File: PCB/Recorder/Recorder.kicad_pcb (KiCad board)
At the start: 2 copper layers, 70 x 70 mm, 54 parts, among them J1 Battery, J2 Reset, J3 TC2030-USB-NL-DS, J4 TF_PUSH, J5 USB-C-Socket-H, Q2 CJ2301, SW1 SW_Push, U1 R, U2 L, U3 TP4054, U4 ME6211C33M5G-N, U5 MAX98357A, U6 ESP32-S3-MINI-1

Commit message: Allow all data on SD card maybe
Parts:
- R14: moved to F.Cu
- moved R14 16.2 mm to (94.0, 108.8), turned to 90 degrees
- moved R10 0.85 mm to (97.5, 108.8)
- moved R13 0.85 mm to (94.9, 108.8)
- moved R3 0.85 mm to (99.2, 108.8)
- moved R11 0.85 mm to (96.6, 108.8)
- moved R12 0.85 mm to (95.8, 108.8)
- moved R9 0.85 mm to (98.3, 108.8)
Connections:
- J4 pad 1: Net-(J4-DAT2) -> SDDAT2
- R14 pad 2: Net-(J4-DAT2) -> SDDAT2
- U6 pad 15: unconnected-(U6-GPIO11-Pad15) -> CHARGING
- U6 pad 16: SDSS -> SDDAT2
- U6 pad 17: SDMOSI -> SDSS
- U6 pad 18: SDSCK -> SDMOSI
- U6 pad 19: SDMISO -> SDSCK
- U6 pad 20: SDDAT1 -> SDMISO
- U6 pad 21: SDCD -> SDDAT1
- U6 pad 22: CHARGING -> SDCD
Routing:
- net SDDAT2: track 0.00 -> 18.1 mm, vias 0 -> 1
- net GND: track 59.6 -> 71.6 mm, vias 17 -> 21
- net CHARGING: track 20.3 -> 27.9 mm, vias 2 -> 4
- net Net-(J2-Pin_2): track 24.8 -> 29.3 mm
- net +3V3: track 135.7 -> 133.4 mm
- net Net-(J4-DAT2): track 1.22 -> 0.00 mm
- net SDCD: track 24.9 -> 25.6 mm
- net D+: track 28.7 -> 28.2 mm

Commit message: Tidy
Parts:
- removed C12: 10uF, RevK:C_0402
- removed C14: 100nF, RevK:C_0402
- removed R4: 634K, RevK:R_0402
- removed TP1: +, RevK:SolderPadSmall
- removed TP2: -, RevK:SolderPadSmall
- removed U5: MAX98357A, RevK:WLP-1.437mmx1.347mm-0.21mm-ball
- moved V2 1.50 mm to (96.5, 110.0)
- moved PCB1 1.00 mm to (96.0, 100.0)
- moved V1 1.00 mm to (96.0, 90.0)
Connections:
- net SDMISO renamed SDDAT0
- net SDMOSI renamed SDCMD
- net SDSCK renamed SDCLK
- net SDSS renamed SDDAT3
- U6 pad 31: SKPWS -> unconnected-(U6-GPIO35-Pad31)
- U6 pad 32: SKPSCK -> unconnected-(U6-GPIO36-Pad32)
- U6 pad 33: SKPSD -> unconnected-(U6-GPIO37-Pad33)
- U6 pad 34: SKPPWR -> unconnected-(U6-GPIO38-Pad34)
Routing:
- net SKPPWR: track 6.62 -> 0.00 mm
- net GND: track 71.6 -> 65.1 mm, vias 21 -> 20
- net SKPWS: track 4.62 -> 0.00 mm, vias 2 -> 0
- net Net-(U5-OUTN): track 4.43 -> 0.00 mm, vias 1 -> 0
- net SKPSD: track 3.77 -> 0.00 mm
- net SKPSCK: track 2.42 -> 0.00 mm
- net +3V3: track 133.4 -> 131.6 mm
- net SCK: track 37.2 -> 35.9 mm
- net SDCD: track 25.6 -> 24.4 mm
- net CHARGING: track 27.9 -> 29.0 mm
- net Net-(U5-OUTP): track 1.02 -> 0.00 mm, vias 1 -> 0
- net D-: track 37.5 -> 36.4 mm
- net Net-(U5-~{SD_MODE}): track 0.60 -> 0.00 mm
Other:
- board text added: "1 8"
- board text added: "12 13 14 15 16 17 18"
- board text added: "41 18"
- board text added: "BTN LED"
- board text added: "Baking not required"
- board text added: "DAT2 DAT3 MOSI SCK DAT0 DAT1 CD"
- board text added: "VBUS CHRG"
- board text added: "Voice Recorder"
- board text removed: "1"
- board text removed: "12 13 14 15 17"
- board text removed: "18"
- board text removed: "35 36"
- board text removed: "37 38"
- board text removed: "41"
- board text removed: "8"
- board text removed: "A"
- board text removed: "Audio"
- board text removed: "B"
- board text removed: "BTN"
- board text removed: "Baking for D1 is not required"
- board text removed: "CHG"
- board text removed: "D P"
- board text removed: "Recorder"
- board text removed: "SPK"
- board text removed: "SS MOSI SCK MISO CD"
- board text removed: "VBUS"
- board text removed: "W C"

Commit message: Clean up
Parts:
- moved C13 5.29 mm to (87.5, 105.5)
- moved C8 3.24 mm to (90.0, 94.5)
- moved J2 2.35 mm to (82.5, 94.0)
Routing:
- net GND: track 65.1 -> 55.3 mm
- net +3V3: track 131.6 -> 122.4 mm
- net Net-(J2-Pin_2): track 29.3 -> 30.9 mm
- net SCK: track 35.9 -> 34.4 mm, vias 2 -> 3
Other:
- board text added: "1"
- board text added: "8"
- board text removed: "1 8"
- board text removed: "BTN LED"
- board text removed: "LED"

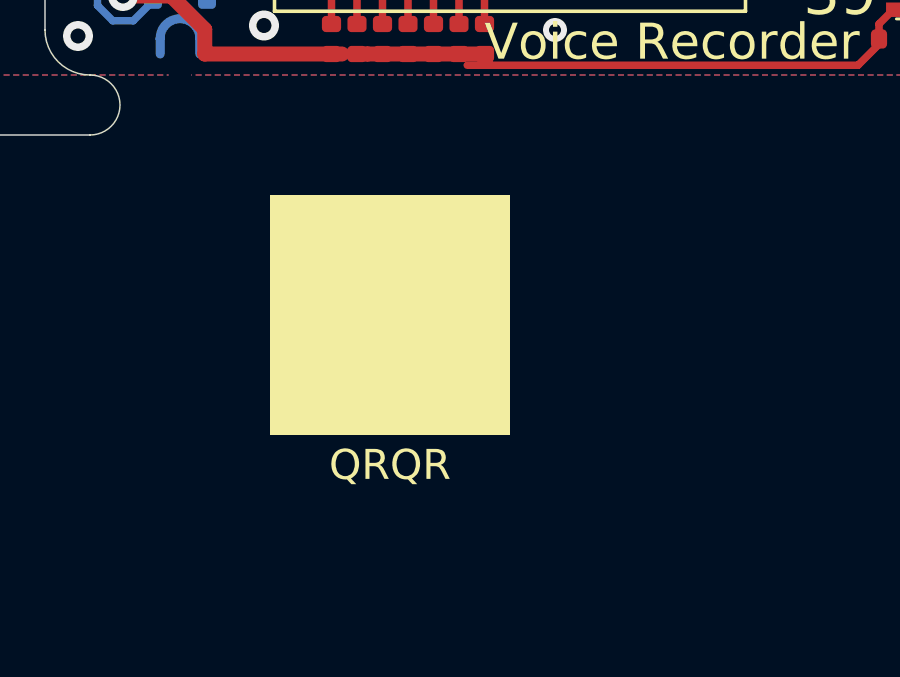
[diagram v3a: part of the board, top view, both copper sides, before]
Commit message: Charging is 11 not 18 FFS
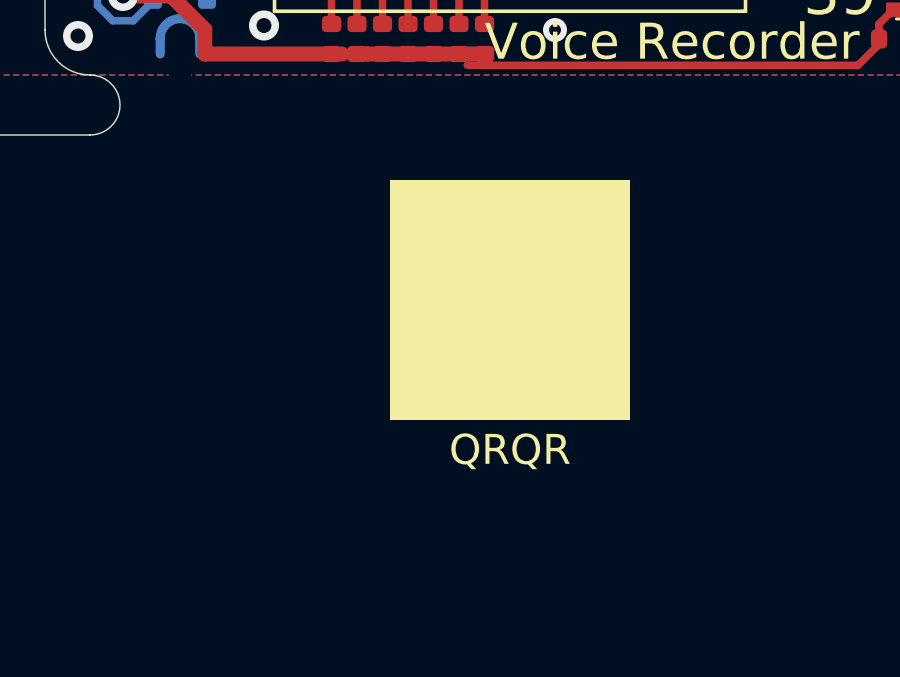
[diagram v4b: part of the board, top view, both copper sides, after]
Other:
- board text added: "41 11"
- board text removed: "41 18"

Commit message: Snap off
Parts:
- moved J2 2.00 mm to (84.5, 94.0), turned to 180 degrees
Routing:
- net BUTTON: track 13.3 -> 9.59 mm
- net SCK: track 34.4 -> 33.7 mm
- net Net-(D4-I): track 23.2 -> 22.7 mm
- net GND: track 55.3 -> 55.1 mm, vias 20 -> 39
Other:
- board text removed: "QRQR"

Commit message: More SS
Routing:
- net GND: track 55.1 -> 55.6 mm
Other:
- board text added: "Made in China for Andrews&Arnold Ltd"
